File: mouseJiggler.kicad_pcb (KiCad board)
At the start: 2 copper layers, 19 x 31 mm, 21 parts, among them J2 48037-0001, U1 ATmega16U2-MU, Y1 16MHz

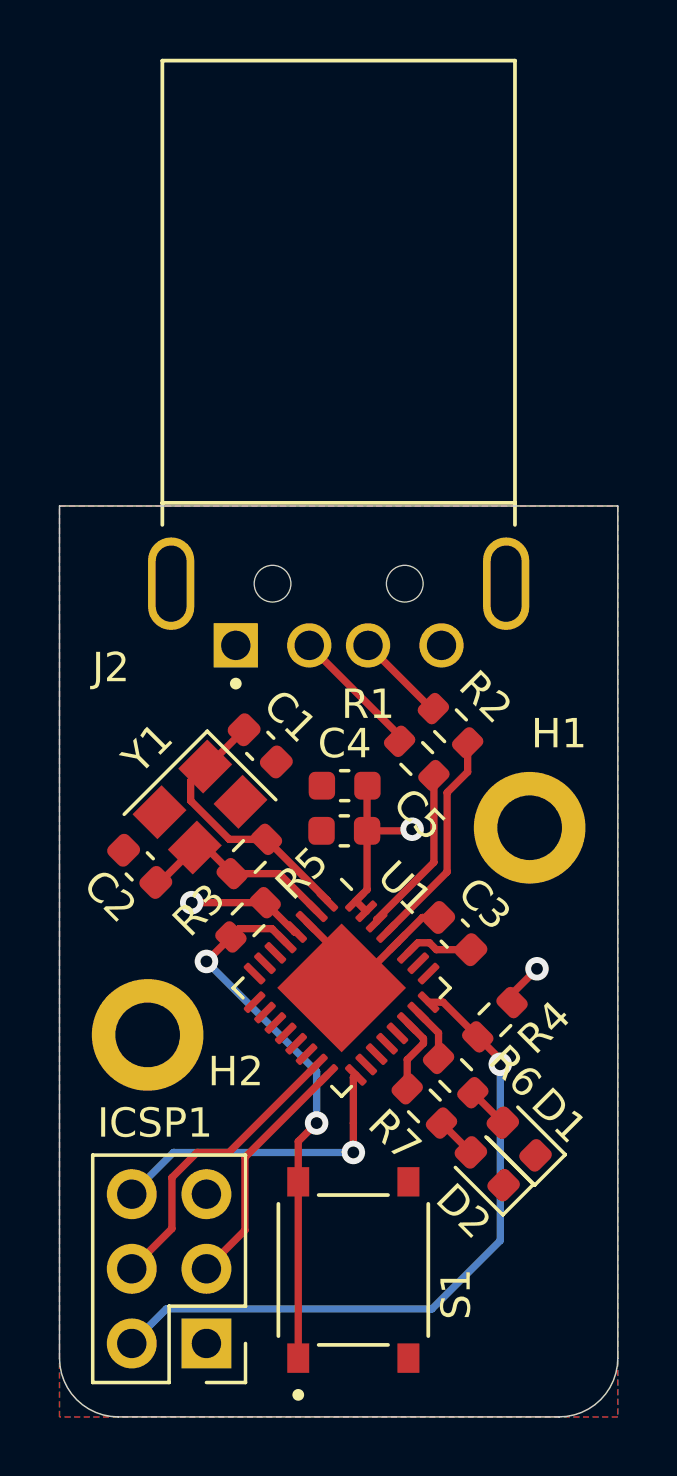
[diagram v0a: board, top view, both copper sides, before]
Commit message: Updated and added silkscreen
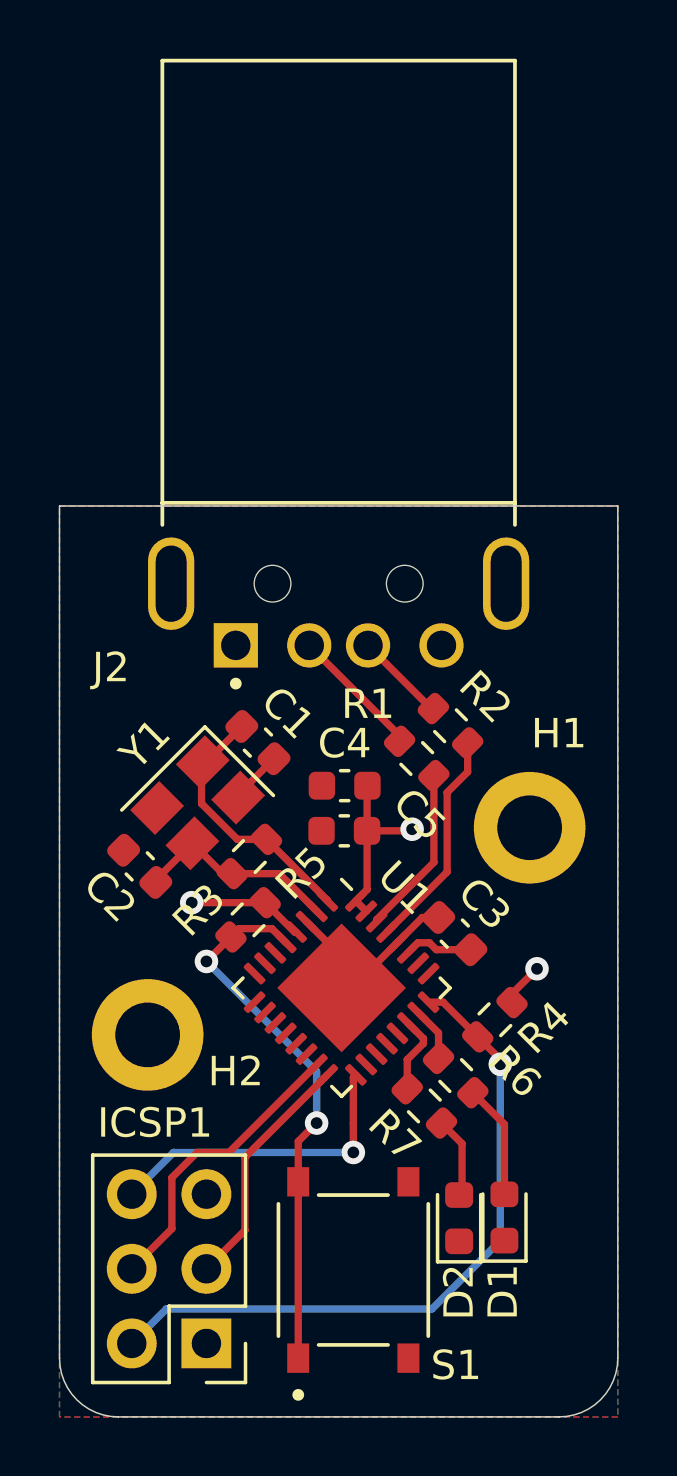
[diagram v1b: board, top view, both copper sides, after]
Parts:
- added G***: LOGO, SnapEDA:donald, B.Cu at (154.2, 103.0)
- moved D1 2.72 mm to (161.1, 116.7), turned to 90 degrees
- moved D2 1.93 mm to (159.6, 116.7), turned to 90 degrees
- moved Y1 0.17 mm to (150.7, 102.6)
- moved C1 0.14 mm to (152.8, 100.6)
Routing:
- net Net-(D1-Pad2): track 1.44 -> 3.90 mm
- net GND: track 7.04 -> 8.87 mm
- net Net-(D2-Pad2): track 1.41 -> 2.78 mm
- net Net-(C2-Pad1): track 6.87 -> 7.57 mm
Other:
- board text added: "<3"
- board text added: "By DanieleVBella"
- board text added: "Designed with"
- board text removed: "By Daniele"
- board text removed: "Designed with <3"

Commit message: Updated USB and silkscreen
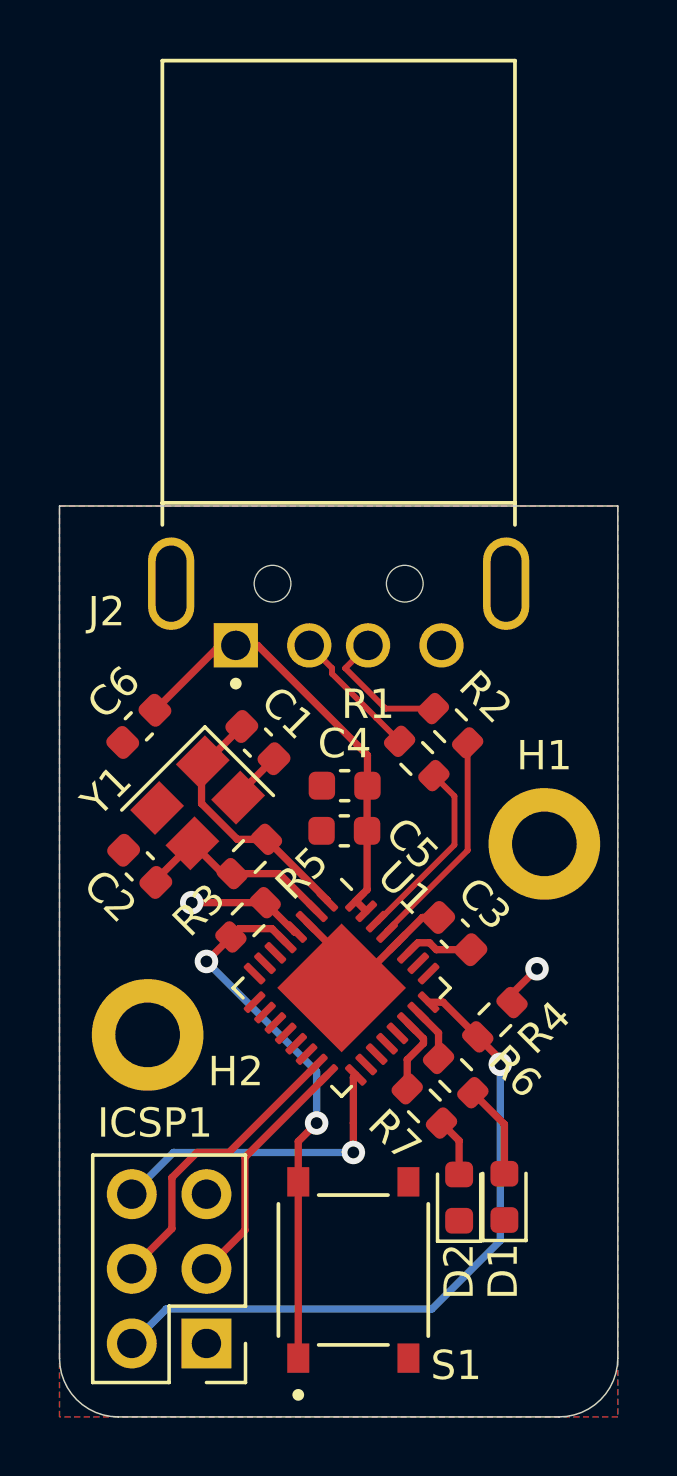
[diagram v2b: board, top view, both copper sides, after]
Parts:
- added C6: 10uF, Capacitor_SMD:C_0603_1608Metric, F.Cu at (148.7, 100.0)
- moved H1 0.74 mm to (162.5, 104.0)
- moved D1 0.70 mm to (161.1, 116.0)
- moved D2 0.70 mm to (159.6, 116.0)
- moved G*** 0.57 mm to (154.6, 103.4)
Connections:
- net Net-(J2-Pad2) renamed /USB_D-
- net Net-(J2-Pad3) renamed /USB_D+
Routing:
- net +5V: track 11.6 -> 21.5 mm, vias 3 -> 2
- net /USB_D+: track 3.11 -> 4.67 mm
- net Net-(D2-Pad2): track 2.78 -> 2.00 mm
- net Net-(D1-Pad2): track 3.90 -> 3.20 mm
- net /D-: track 5.78 -> 6.38 mm
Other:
- board text added: "Designed with <3"
- board text added: "Mini-Keyboard Hacker"
- board text removed: "<3"
- board text removed: "Designed with"

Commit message: Made final changes to silkscreen
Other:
- board text added: "Da DanieleVBella"
- board text added: "Paperino Di Gomma"
- board text added: "Progettato con <3"
- board text removed: "By DanieleVBella"
- board text removed: "Designed with <3"
- board text removed: "Mini-Keyboard Hacker"
